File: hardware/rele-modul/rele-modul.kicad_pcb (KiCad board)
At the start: 4 copper layers, 68 x 86.5 mm, 80 parts, among them J1 DEBUG, J100 24V IN, J101 RELÉ 1, J102 RELÉ 2, J103 RELÉ 3, J104 RELÉ 4, J105 SCT-013, J2 BUS_IN, J3 BUS_OUT, J4 BŐVÍTŐ, K1 RTD14024, K2 RTD14024, K3 RTD14024, K4 RTD14024, U101 ULN2803ADWR, U2 TCAN1044AVDRQ1, U3 ESD2CAN24-Q1, U5 AP2112K-3.3TRG1, U6 STM32F303RET6, Y1 8MHz

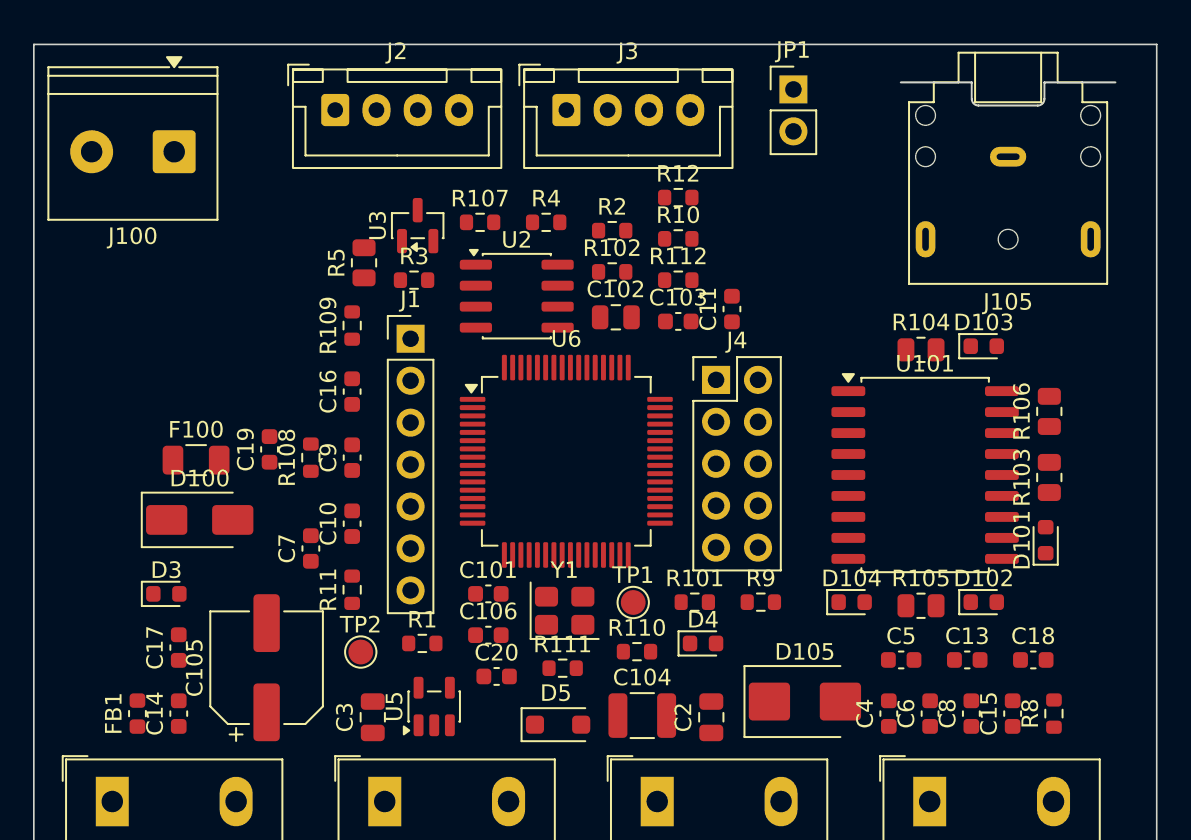
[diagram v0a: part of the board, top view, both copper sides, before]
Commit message: Hardver: szakértői javítások (D74–D77), STM32L433 + SN65HVD230 + GND-ági polaritásvédelem (D78–D81), teljes ellenőrzés
- D74–D77: busz-GND ellenállás, CAN-fojtó-hely, TVS a +5V_BUCK-on és a VUSB-n, bemenetvédelem,
  230 V-os és antenna-tiltás a NYÁK-on, SCT-jack footprint
- D78–D80: modul-MCU STM32L433RCT3 (VIN_SENSE PB1, LED: TIM15/TIM16, I_SENSE PA3), modul-transceiver
  SN65HVD230, N-FET a GND-ágban (vezérlő Q1, LED Q201, relé Q100), MCP9701A, táp-LED a +5V-ról,
  2 oz a LED-/relémodulon, AP2112K marad; D81 javaslat (TPD4E02B04 a bemeneteken)
- CubeMX-projektek L433-ra, fejsoros kódgenerálással ellenőrizve (minden periféria inicializálódik)
- gen/ellenorzes.py (ERC, láb ↔ pad, modulmag, CubeMX, polaritásvédelem, NYÁK ↔ rajz, DRC) – 0 hiba
- gen/bom.sh + bom/*.csv darabjegyzék; docs/komponenslista.md a konzulensnek
- kontextus: DONTESEK D74–D81, specifikációk, ATTEKINTES, NAPLO, beszerzési lista; alkatrészkészlet-jegyzet (claude.ai)

Co-Authored-By: Claude Opus 5.5 <noreply@anthropic.com>
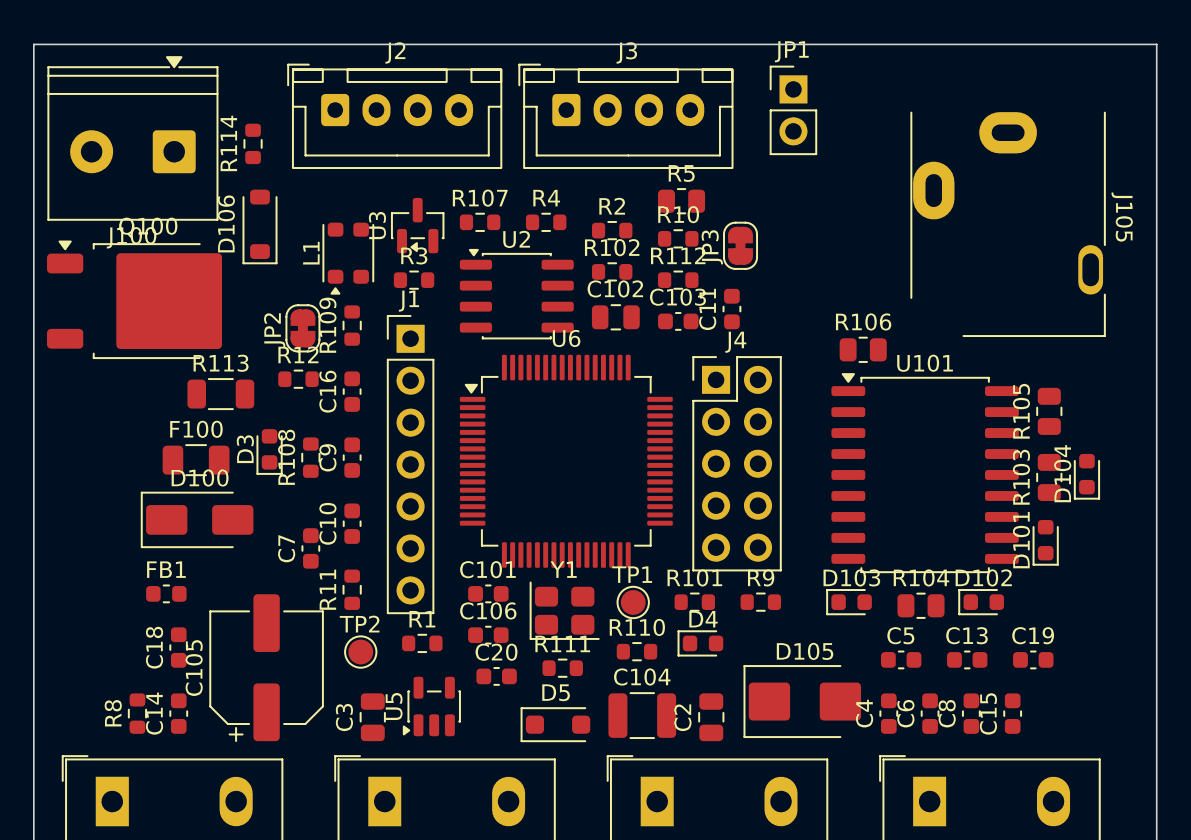
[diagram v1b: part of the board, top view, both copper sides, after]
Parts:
- removed C17: 100n, Capacitor_SMD:C_0603_1608Metric
- added D106: BZT52C15, Diode_SMD:D_SOD-123, F.Cu at (113.7, 110.9)
- added JP2: áthidaló, Jumper:SolderJumper-2_P1.3mm_Bridged_RoundedPad1.0x1.5mm, F.Cu at (116.3, 117.2)
- added JP3: áthidaló, Jumper:SolderJumper-2_P1.3mm_Bridged_RoundedPad1.0x1.5mm, F.Cu at (142.8, 112.2)
- added L1: DNP, Inductor_SMD:L_CommonModeChoke_Coilank_ACM3225, F.Cu at (119.0, 112.6)
- added Q100: IRFR120N, Package_TO_SOT_SMD:TO-252-2, F.Cu at (106.9, 115.5)
- added R113: 0R, Resistor_SMD:R_1206_3216Metric, F.Cu at (111.3, 121.2)
- added R114: 10k, Resistor_SMD:R_0603_1608Metric, F.Cu at (113.3, 106.0)
- J105: footprint Connector_Audio:Jack_3.5mm_CUI_SJ1-3523N_Horizontal -> Connector_Audio:Jack_3.5mm_CUI_SJ1-3513N_Horizontal
- U2: value TCAN1044AVDRQ1 -> SN65HVD230D
- U6: value STM32F303RET6 -> STM32L433RCT3
- moved R8 55.5 mm to (106.3, 140.5)
- moved C18 51.8 mm to (108.8, 136.5), turned to 90 degrees
- moved C19 48.0 mm to (160.5, 137.3), turned to 0 degrees
- moved R12 25.5 mm to (116.0, 120.3)
- moved R5 19.6 mm to (139.2, 109.5), turned to 0 degrees
- moved D103 17.4 mm to (149.5, 133.8)
- moved D104 16.2 mm to (163.8, 126.0), turned to 90 degrees
- moved R104 15.5 mm to (153.7, 134.0)
- moved R105 14.1 mm to (161.5, 122.2), turned to 90 degrees
- moved R106 11.9 mm to (150.2, 118.5), turned to 0 degrees
- moved D3 10.8 mm to (114.3, 124.5), turned to 90 degrees
- moved FB1 7.46 mm to (108.0, 133.3), turned to 0 degrees
- moved J105 1.45 mm to (159.0, 105.3), turned to -90 degrees
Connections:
- C18 pad 1: +5V -> +3V3
- C19 pad 1: +5V -> +3V3
- J100 pad 2: GND -> /GND_IN
- J2 pad 2: GND -> /GND_BUS
- J3 pad 2: GND -> /GND_BUS
- R8 pad 1: +3V3 -> +5V
- U2 pad 3: +5V -> +3V3
- U2 pad 5: +3V3 -> unconnected-(U2-Vref-Pad5)
- U2 pad 6: /modulmag/CAN_L -> /modulmag/CAN_L_T
- U2 pad 7: /modulmag/CAN_H -> /modulmag/CAN_H_T
- U6 pad 27: unconnected-(U6-PB1-Pad27) -> /VIN_SENSE
- U6 pad 30: /VIN_SENSE -> /modulmag/PB11
- U6 pad 37: /modulmag/PC6 -> unconnected-(U6-PC6-Pad37)
- U6 pad 38: /modulmag/PC7 -> unconnected-(U6-PC7-Pad38)
- U6 pad 39: /modulmag/PC8 -> unconnected-(U6-PC8-Pad39)
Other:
- board text added: "≥ 8 mm: SELV-réz egyik rétegen sem (a 230 V-os pad 59.6 mm-nél kezdődik)"

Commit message: Hardver: determinisztikus UUID-k – a NYÁK-footprintek újra a rajzi szimbólumokra mutatnak
- kigen: a szimbólum-UUID a projekt + hivatkozási jel alapján (uuid5), a többi elemé laponként sorszámból –
  két generálás bájtra azonos fájlt ad, és az újragenerálás nem töri el a „Update PCB from Schematic”-ot (D67)
- a négy NYÁK újragenerálva: mind a 581 footprint a saját szimbólumára mutat (előtte egy sem)
- ellenorzes.py: új ellenőrzés a NYÁK ↔ rajz szimbólum-kapcsolatra; teljes futás: 0 hiba
- README, NAPLO

Co-Authored-By: Claude Opus 5.5 <noreply@anthropic.com>
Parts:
- moved C19 51.8 mm to (108.8, 136.5), turned to 90 degrees
- moved C18 50.7 mm to (159.3, 140.5)
- moved C15 50.5 mm to (108.8, 140.5)
- moved D3 48.0 mm to (160.5, 137.3), turned to 0 degrees
- moved R11 29.0 mm to (139.0, 111.8), turned to 0 degrees
- moved R2 27.5 mm to (123.5, 136.3)
- moved R9 26.4 mm to (131.0, 110.8)
- moved R10 22.6 mm to (144.0, 133.8)
- moved R1 17.7 mm to (116.0, 120.3)
- moved R108 17.6 mm to (127.0, 110.8), turned to 0 degrees
- moved R109 16.0 mm to (119.3, 133.0)
- moved C14 15.1 mm to (116.0, 127.3), turned to 0 degrees
- moved R3 12.4 mm to (135.0, 111.3)
- moved FB1 11.2 mm to (114.3, 124.0), turned to 90 degrees
- moved R107 9.96 mm to (119.3, 117.0), turned to 90 degrees
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
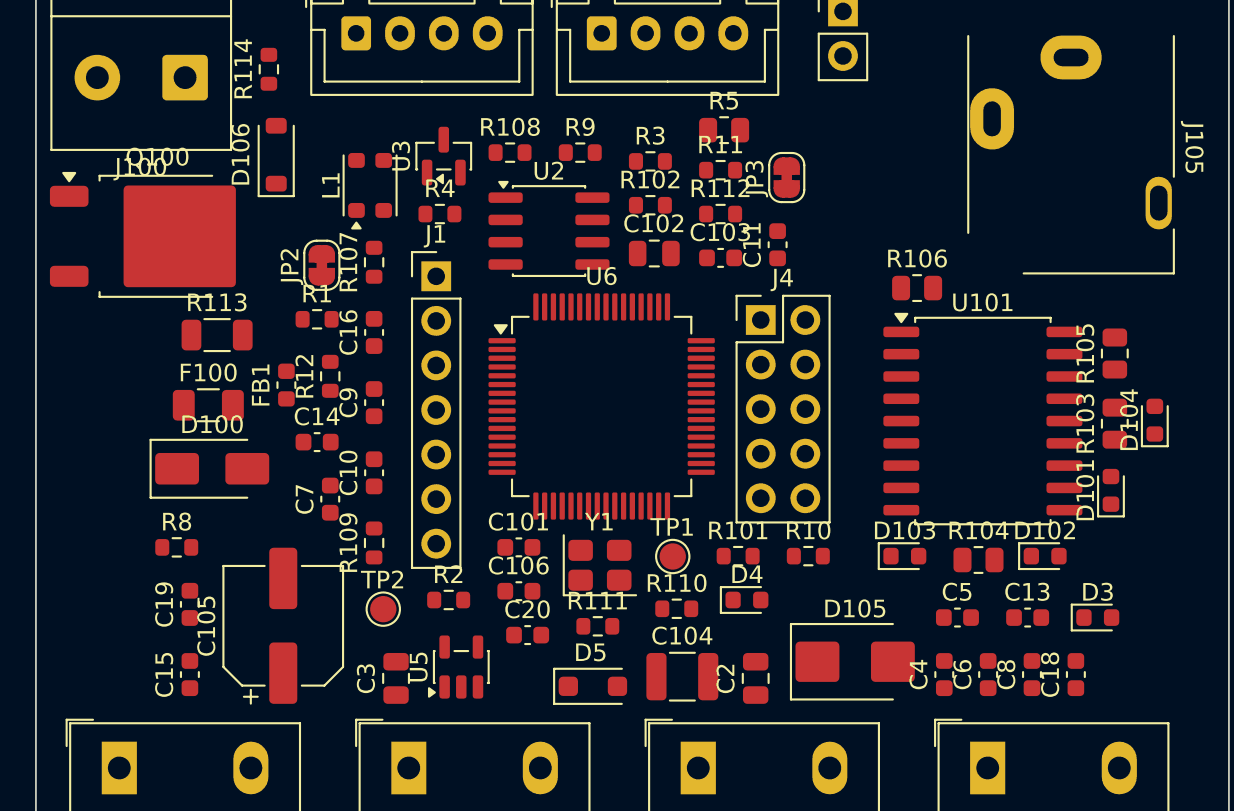
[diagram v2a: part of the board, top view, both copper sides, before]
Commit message: Hardver: 1 oz + fedetlen nagyáramú sávok (D82), reprodukálható rajzgenerálás; kontextus: rajzlezárás
- D82: minden NYÁK 1 oz (a JLC 2 oz-nál ≥ 0,2 mm szélességet/távolságot kér, az LQFP-64 rése épp ennyi);
  a nagyáramú sávok fedetlenek, utólag ónozva / vezetékkel – leírás a NYAK-ELOKESZITES-ben (a söntöt nem ónozni)
- LED- és relé-NYÁK újragenerálva 1 oz-zal; az ellenőrző az 1 oz-ot figyeli
- kigen: minden egységpéldány a szimbólum összes lábát felsorolja → a „sch upgrade” nem pótol véletlen UUID-t,
  mind az öt rajz bájtra reprodukálható
- kontextus: ATTEKINTES (rajzok lezárva 10-22), UTEMTERV, NAPLO, DONTESEK D82; komponenslista állapotsora

Co-Authored-By: Claude Opus 5.5 <noreply@anthropic.com>
Claude-Session: https://claude.ai/code/session_01KVtZMUPbtveTXy9VyJshyt
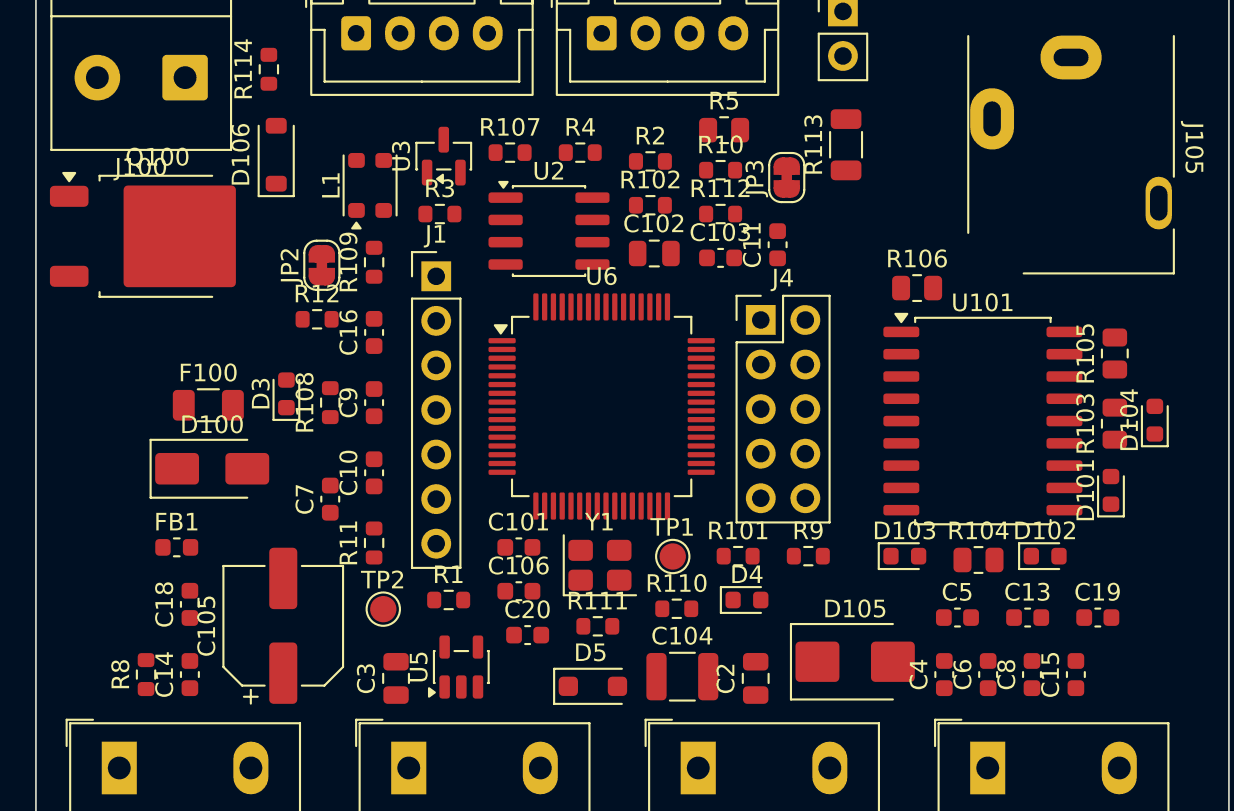
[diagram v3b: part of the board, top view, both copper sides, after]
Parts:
- moved C19 51.8 mm to (160.5, 137.3), turned to 0 degrees
- moved C18 50.7 mm to (108.8, 136.5)
- moved C15 50.5 mm to (159.3, 140.5)
- moved D3 48.0 mm to (114.3, 124.5), turned to 90 degrees
- moved R113 37.5 mm to (146.2, 110.3), turned to 90 degrees
- moved R11 29.0 mm to (119.3, 133.0), turned to 90 degrees
- moved R2 27.5 mm to (135.0, 111.3)
- moved R9 26.4 mm to (144.0, 133.8)
- moved R10 22.6 mm to (139.0, 111.8)
- moved R1 17.7 mm to (123.5, 136.3)
- moved R108 17.6 mm to (116.8, 125.0), turned to 90 degrees
- moved R109 16.0 mm to (119.3, 117.0)
- moved C14 15.1 mm to (108.8, 140.5), turned to 90 degrees
- moved R3 12.4 mm to (123.0, 114.3)
- moved FB1 11.2 mm to (108.0, 133.3), turned to 0 degrees
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
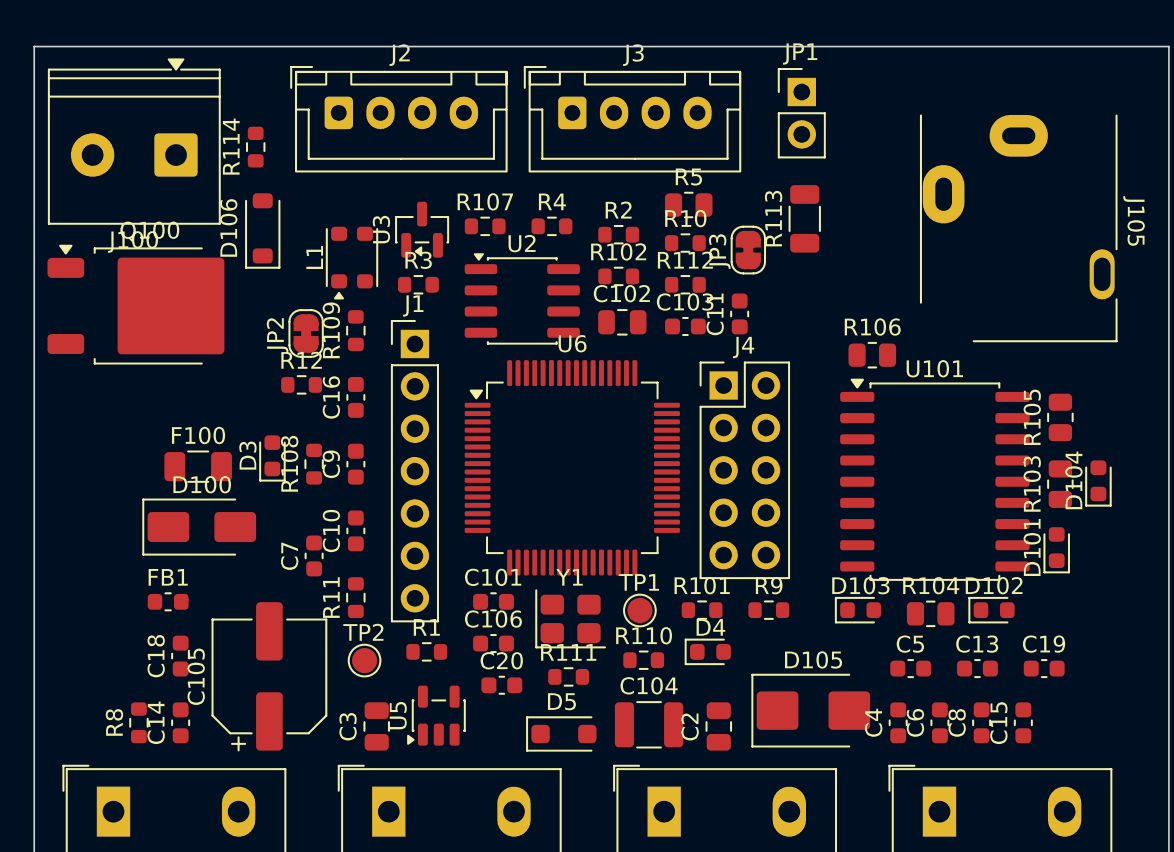
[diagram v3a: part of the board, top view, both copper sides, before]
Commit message: Hardver: legolcsóbb beszerzés (D84) – Hestore + DigiKey, a rajz a kapható típusokra igazítva; beszerzési lista
- gen/beszerzes.py → bom/beszerzes.csv: BOM-tételenként forrás, Hestore-kód, nettó ár, készlet
- J1/J100 Degson DG250, J201 DG128 (15 A), J202–J204 KF128, F201 15 A; L1/L3 HPI0630 (saját footprint);
  R209 CRE2512; C40/C41 12 pF; ESP32-C6-WROOM-1-N8; SS56C, BAT54HT1G, STPS3L60U, BLM18EG221
- NYÁK-ok újragenerálva (a layout még nem indult el); bekötés változatlan, ellenorzes.py: 0 hiba
- SAMPLE-KERESEK: az NTMFS5C604NL nincs kézben (javítva)

Co-Authored-By: Claude Opus 5.5 <noreply@anthropic.com>
Claude-Session: https://claude.ai/code/session_01KVtZMUPbtveTXy9VyJshyt
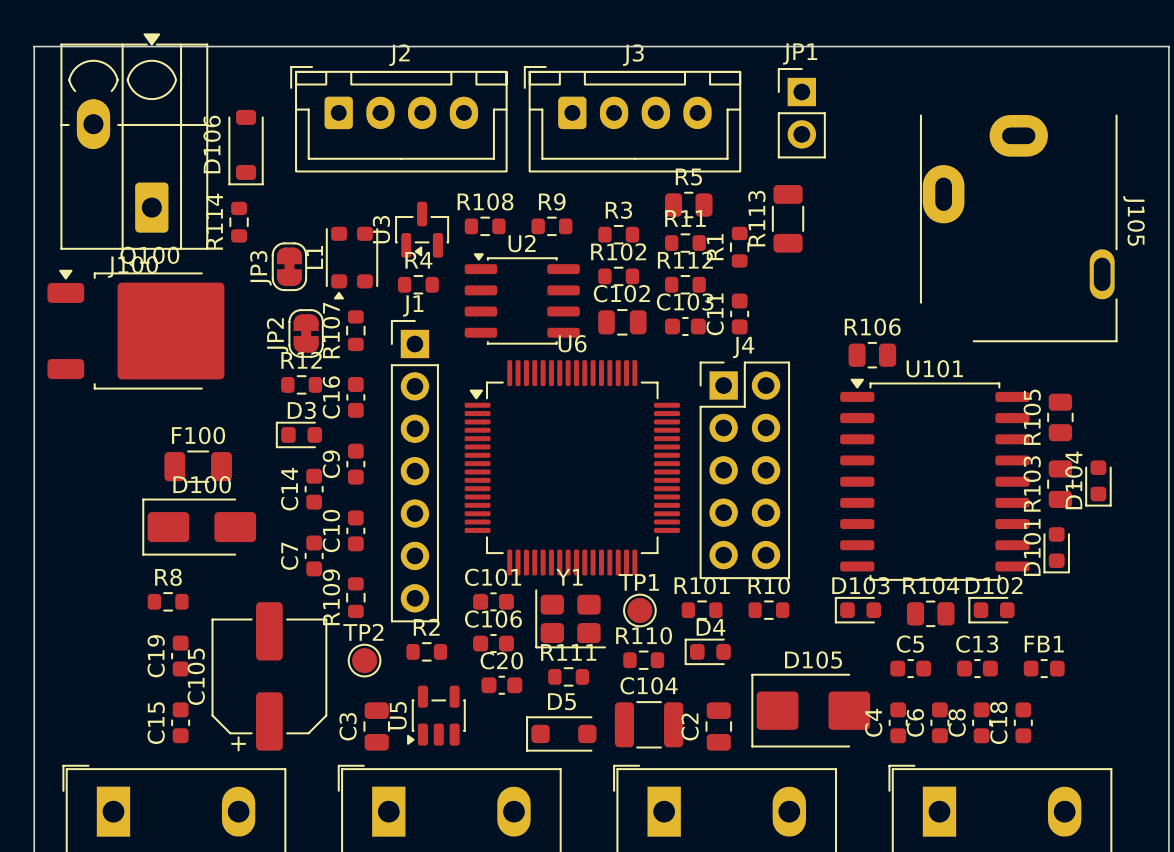
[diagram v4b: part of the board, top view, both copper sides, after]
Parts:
- FB1: value ferrit ≤0,1Ω -> BLM18EG221
- J100: footprint TerminalBlock_Phoenix:TerminalBlock_Phoenix_PT-1,5-2-5.0-H_1x02_P5.00mm_Horizontal -> TerminalBlock_Degson:TerminalBlock_Degson_DG250-3.5-02P_1x02_P3.50mm_45Degree
- moved FB1 52.7 mm to (160.5, 137.3)
- moved C19 51.8 mm to (108.8, 136.5), turned to 90 degrees
- moved C18 50.7 mm to (159.3, 140.5)
- moved C15 50.5 mm to (108.8, 140.5)
- moved R1 30.7 mm to (142.3, 112.0), turned to 90 degrees
- moved R11 29.0 mm to (139.0, 111.8), turned to 0 degrees
- moved R2 27.5 mm to (123.5, 136.3)
- moved JP3 27.5 mm to (115.3, 113.2)
- moved R9 26.4 mm to (131.0, 110.8)
- moved R10 22.6 mm to (144.0, 133.8)
- moved R108 17.6 mm to (127.0, 110.8), turned to 0 degrees
- moved C14 16.1 mm to (116.8, 126.5)
- moved R109 16.0 mm to (119.3, 133.0)
- moved R3 12.4 mm to (135.0, 111.3)
- moved R107 9.96 mm to (119.3, 117.0), turned to 90 degrees
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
